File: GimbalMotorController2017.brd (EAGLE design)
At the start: 96.6 x 79.2 mm, 125 parts, among them J1 SL03THROUGH_HOLE, J3 APP_2POS_CONFIG5V_HORIZ, Q7 MOSFET-PCHANNEL, Q8 MOSFET-PCHANNEL, Q9 MOSFET-NCHANNELAO3404A, U1 NUP4201MR6, U2 MAX3232D, U3 CSD18533Q5A, U4 CSD18533Q5A, U5 CSD18533Q5A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

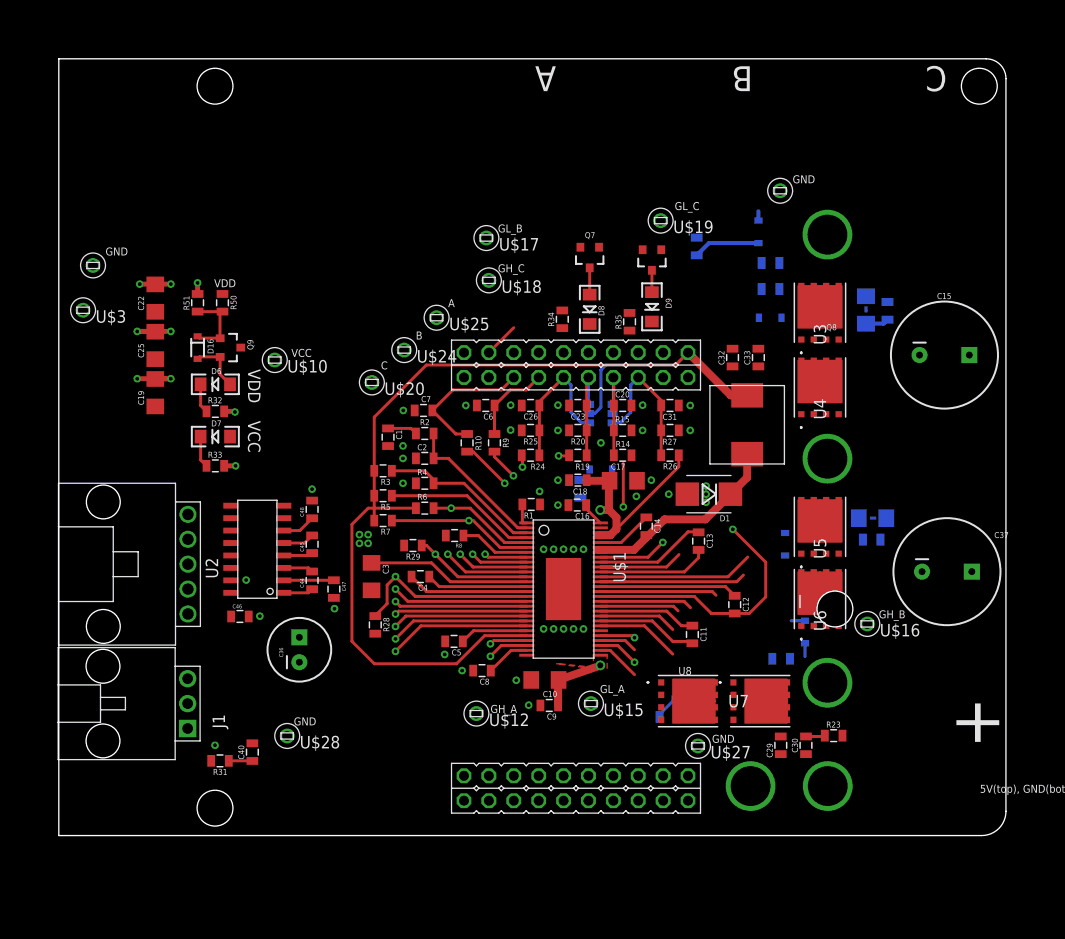
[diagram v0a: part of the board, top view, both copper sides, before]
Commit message: Routed traces for external connections, caps, and a few diodes. Most traces completed except for fet traces.
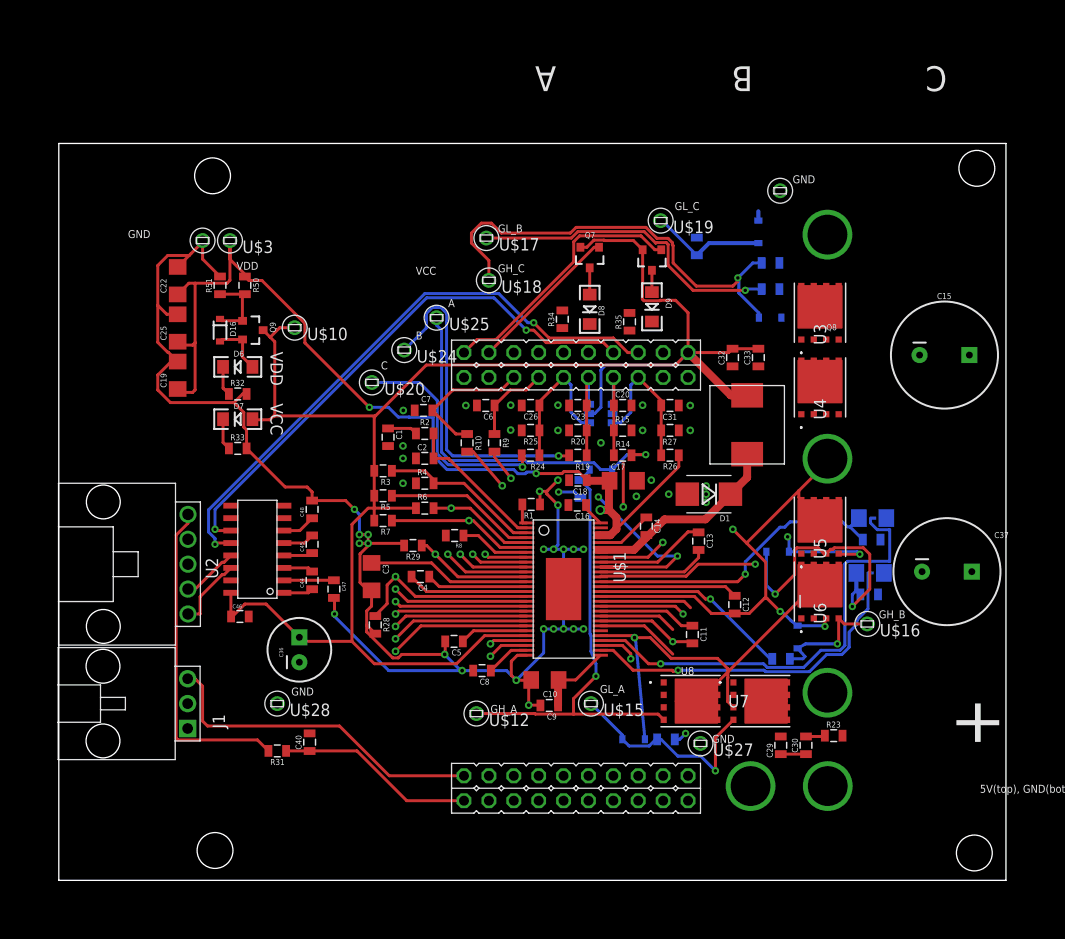
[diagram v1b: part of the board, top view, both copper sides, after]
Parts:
- moved C24 29.0 mm to (82.0, 24.9), turned to 180 degrees
- moved SH1 26.9 mm to (82.1, 27.1), turned to 0 degrees
- moved R18 26.8 mm to (82.1, 27.1), turned to 0 degrees
- moved U$3 16.6 mm to (16.8, 61.0)
- moved U$26 11.5 mm to (14.0, 61.0)
- moved D12 6.71 mm to (58.0, 10.1)
- moved R31 5.93 mm to (21.6, 8.89)
- moved C40 5.93 mm to (24.9, 9.78)
- moved U$10 3.88 mm to (23.4, 52.1)
- moved U$28 3.45 mm to (21.6, 13.7)
- moved Q9 2.90 mm to (19.1, 51.8)
- moved D16 2.90 mm to (15.7, 51.8)
- moved R32 2.90 mm to (17.6, 45.3)
- moved R50 2.90 mm to (18.3, 56.4)
- moved C19 2.90 mm to (11.4, 47.2)
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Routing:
- net GND: track 18.0 -> 158.3 mm, vias 55 -> 43
- net PVDD: track 29.7 -> 125.0 mm, vias 2 -> 3
- net VCC: track 143.6 -> 214.1 mm
- net N$15: track 0.00 -> 70.2 mm, vias 0 -> 3
- net UART_RX: track 0.00 -> 60.9 mm, vias 0 -> 2
- net UART_TX: track 0.00 -> 55.6 mm, vias 0 -> 2
- net SH_B: track 50.1 -> 102.8 mm, vias 2 -> 4
- net N$13: track 0.00 -> 46.2 mm, vias 0 -> 1
- net N$17: track 0.00 -> 46.0 mm, vias 0 -> 1
- net SP1: track 3.88 -> 46.0 mm, vias 0 -> 1
- net SL_A: track 36.2 -> 75.2 mm, vias 1 -> 2
- net SH_A: track 26.3 -> 63.9 mm, vias 1 -> 2
- net SL_B: track 22.2 -> 59.0 mm, vias 1 -> 4
- net PWM_IN_NO_FILTER: track 0.00 -> 34.4 mm
- net N$34: track 0.00 -> 33.3 mm
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- removed copper zone on layer 1, net PVDD
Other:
- board size 96.6 x 79.2 mm -> 96.6 x 75.2 mm
